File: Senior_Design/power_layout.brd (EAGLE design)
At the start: 105.8 x 35 mm, 70 parts, among them IC1 MIC29302WU, J1 AU-Y1008-2, J1[SIMCARD] 78646-3001, J2 U.FL-R-SMT-1(01), J4[GROVE] 640456-4, T1 BCX70SMD, T2 BCX70SMD, U1 SIM7000E, U2 TUSB2046BVFR, U3 PCA9306DQER, U4 TPS2044BDR, X1 332-04

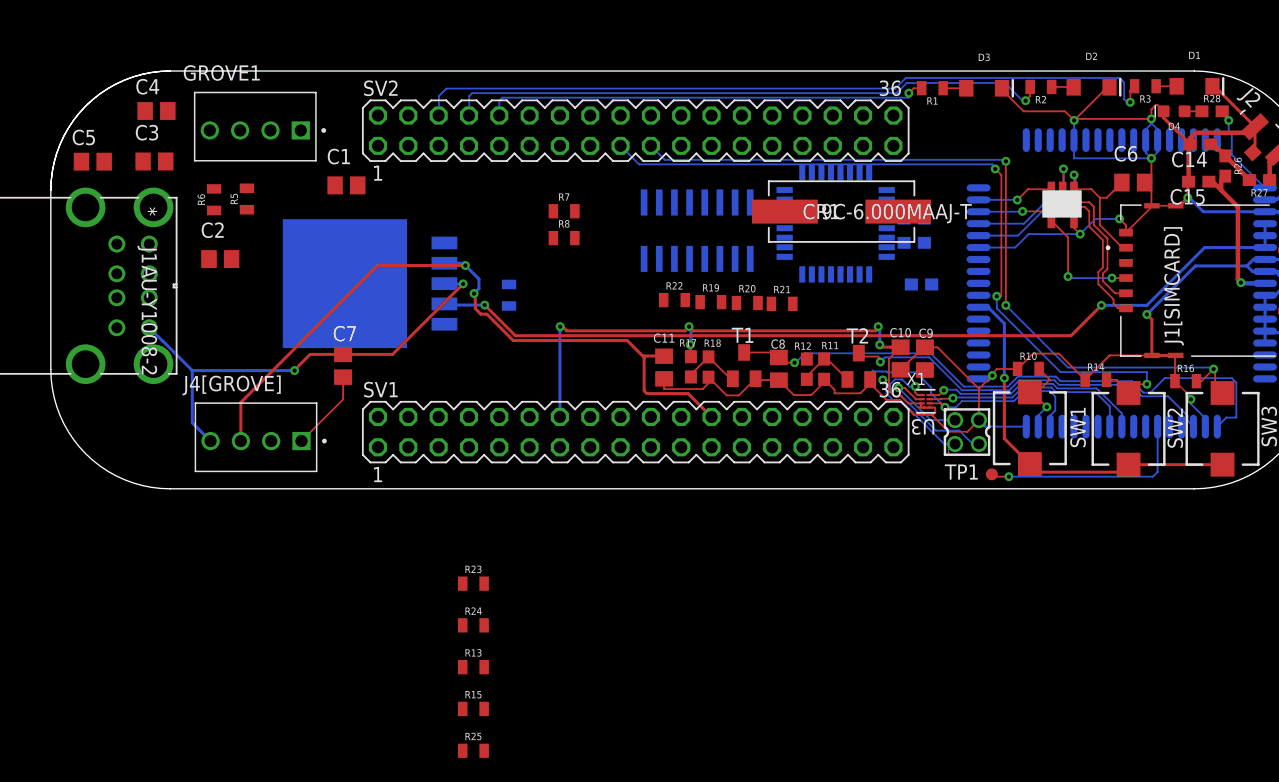
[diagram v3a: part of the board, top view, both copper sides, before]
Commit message: Add files via upload
Final Design files prior to CDR!
Includes schematic and layout
-Needs final review prior to ordering
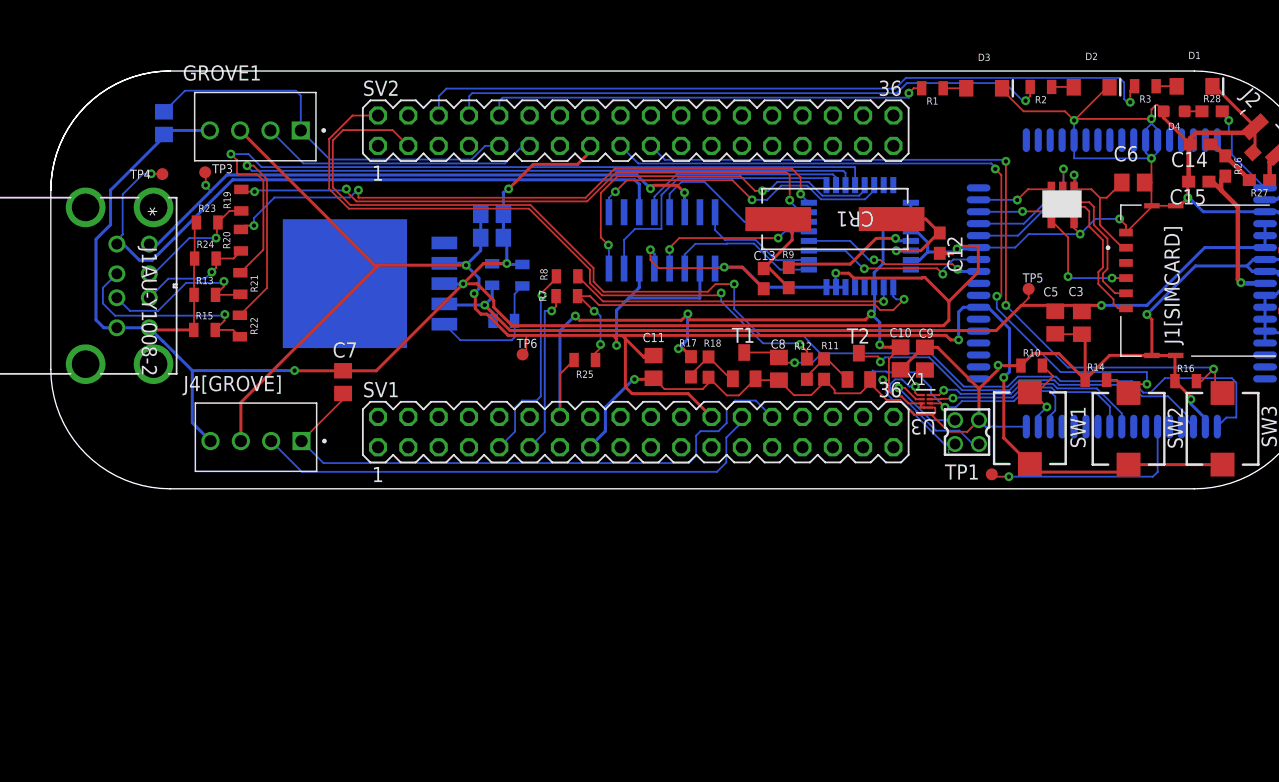
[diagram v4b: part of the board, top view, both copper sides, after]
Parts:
- added TP3, TP4, TP5, TP6: TPTP10R, testpad:TP10R
- moved C5 81.7 mm to (84.1, 13.9), turned to 270 degrees
- moved C3 78.9 mm to (86.4, 13.9), turned to 270 degrees
- moved R21 45.4 mm to (15.9, 17.2), turned to 270 degrees
- moved R20 42.7 mm to (15.9, 20.8), turned to 90 degrees
- moved R19 40.3 mm to (16.0, 24.2), turned to 90 degrees
- moved R15 38.9 mm to (12.9, 13.3)
- moved R13 38.5 mm to (12.9, 16.2)
- moved R24 38.1 mm to (12.9, 19.3)
- moved R23 37.6 mm to (13.1, 22.3)
- moved R22 36.5 mm to (15.8, 13.6), turned to 270 degrees
- moved R25 34.0 mm to (44.7, 10.8), turned to 180 degrees
- moved C4 29.4 mm to (37.0, 23.0), flipped to the bottom, turned to 180 degrees
- moved R6 24.1 mm to (37.0, 17.9), flipped to the bottom, turned to 270 degrees
- moved R5 23.8 mm to (38.0, 14.1), flipped to the bottom, turned to 0 degrees
- moved C13 13.6 mm to (59.7, 17.6), flipped to the top, turned to 270 degrees
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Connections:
- net +5V: now also TP6.TP
- net MODEM_POWER: now also TP5.TP
- net OUT2: now also TP3.TP
- net OUT3: now also TP4.TP
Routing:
- net GND: track 252.9 -> 433.2 mm, vias 13 -> 20
- net +5V: track 92.5 -> 167.0 mm, vias 3 -> 5
- net N$22: track 0.00 -> 67.0 mm, vias 0 -> 1
- net N$23: track 0.00 -> 65.9 mm, vias 0 -> 1
- net PWRKEY: track 49.5 -> 109.7 mm, vias 1 -> 2
- net OUT3: track 0.00 -> 58.3 mm, vias 0 -> 1
- net SLEEP: track 0.00 -> 56.8 mm, vias 0 -> 2
- net N$20: track 0.00 -> 53.0 mm, vias 0 -> 3
- net N$19: track 0.00 -> 52.0 mm, vias 0 -> 3
- net OUT2: track 0.00 -> 51.5 mm, vias 0 -> 3
- net I2C2_SDA: track 0.00 -> 43.9 mm
- net I2C2_SCL: track 6.80 -> 50.0 mm
- net N$10: track 0.00 -> 36.3 mm, vias 0 -> 3
- net I2C1_SCL: track 0.00 -> 33.4 mm
- net PWRON4: track 0.00 -> 31.2 mm, vias 0 -> 2
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
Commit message: Added Pre-PCB Review Changes
Polishing of post-CDR design
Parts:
- added R29, R30, R31, R32: 4700, SparkFun-Resistors:0805
- added R33: 220k, SparkFun-Resistors:0603
- added SJ1: (no value), jumper:SJW
- moved R8 0.70 mm to (42.7, 18.2)
- moved R14 0.57 mm to (87.0, 9.38)
- moved R7 0.51 mm to (42.7, 16.3)
- moved C15 0.43 mm to (95.7, 25.7)
- moved R16 0.36 mm to (95.0, 9.37)
- moved R18 0.33 mm to (55.4, 10.2)
- moved C5 0.31 mm to (83.8, 13.9)
- moved C14 0.31 mm to (96.0, 28.9)
- moved R11 0.20 mm to (65.0, 10.00)
- moved R26 0.20 mm to (98.6, 27.0)
- moved R17 0.15 mm to (53.8, 10.2)
- moved R10 0.09 mm to (82.1, 10.4)
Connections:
- new net N$21: R33.2, U3.7, U3.8
- net +5V: now also IC1.1; no longer GROVE1.3, J4[GROVE].3
- net 3.3V: now also GROVE1.3, J4[GROVE].3, R29.2, R30.2, R31.2, R32.2, R33.1, SJ1.1; no longer U3.7, U3.8
- net I2C1_SCL: now also R29.1
- net I2C1_SDA: now also R30.1
- net I2C2_SCL: now also R31.1
- net I2C2_SDA: now also R32.1
- net MODEM_POWER: now also SJ1.2
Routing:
- net 3.3V: track 78.6 -> 148.8 mm, vias 6 -> 5
- net +5V: track 167.0 -> 125.7 mm
- net GND: track 433.2 -> 443.6 mm
- net MODEM_POWER: track 80.8 -> 87.9 mm, vias 2 -> 3
- net I2C1_SDA: track 23.5 -> 28.5 mm
- net I2C1_SCL: track 33.4 -> 38.2 mm
- net I2C2_SCL: track 50.0 -> 54.7 mm
- net I2C2_SDA: track 43.9 -> 48.3 mm
- net N$21: track 0.00 -> 3.00 mm
- net 1.8V: track 21.7 -> 20.2 mm
- net N$12: track 27.7 -> 28.4 mm
- net PB2: track 64.6 -> 65.2 mm
- net DM0: track 17.1 -> 17.7 mm
- net N$10: track 36.3 -> 36.9 mm
- net PRE_ANT: track 13.1 -> 13.6 mm
